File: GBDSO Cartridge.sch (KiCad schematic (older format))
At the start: 73 parts, among them J1 MJ-3523-SMT-TR, J2 MJ-3523-SMT-TR, J3 EdgeConnector, P1 100k, P2 100k, SW1 SW_SPDT, SW2 SW_SPDT, U1 TL062, U2 DS1267_SOIC, U3 TL062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

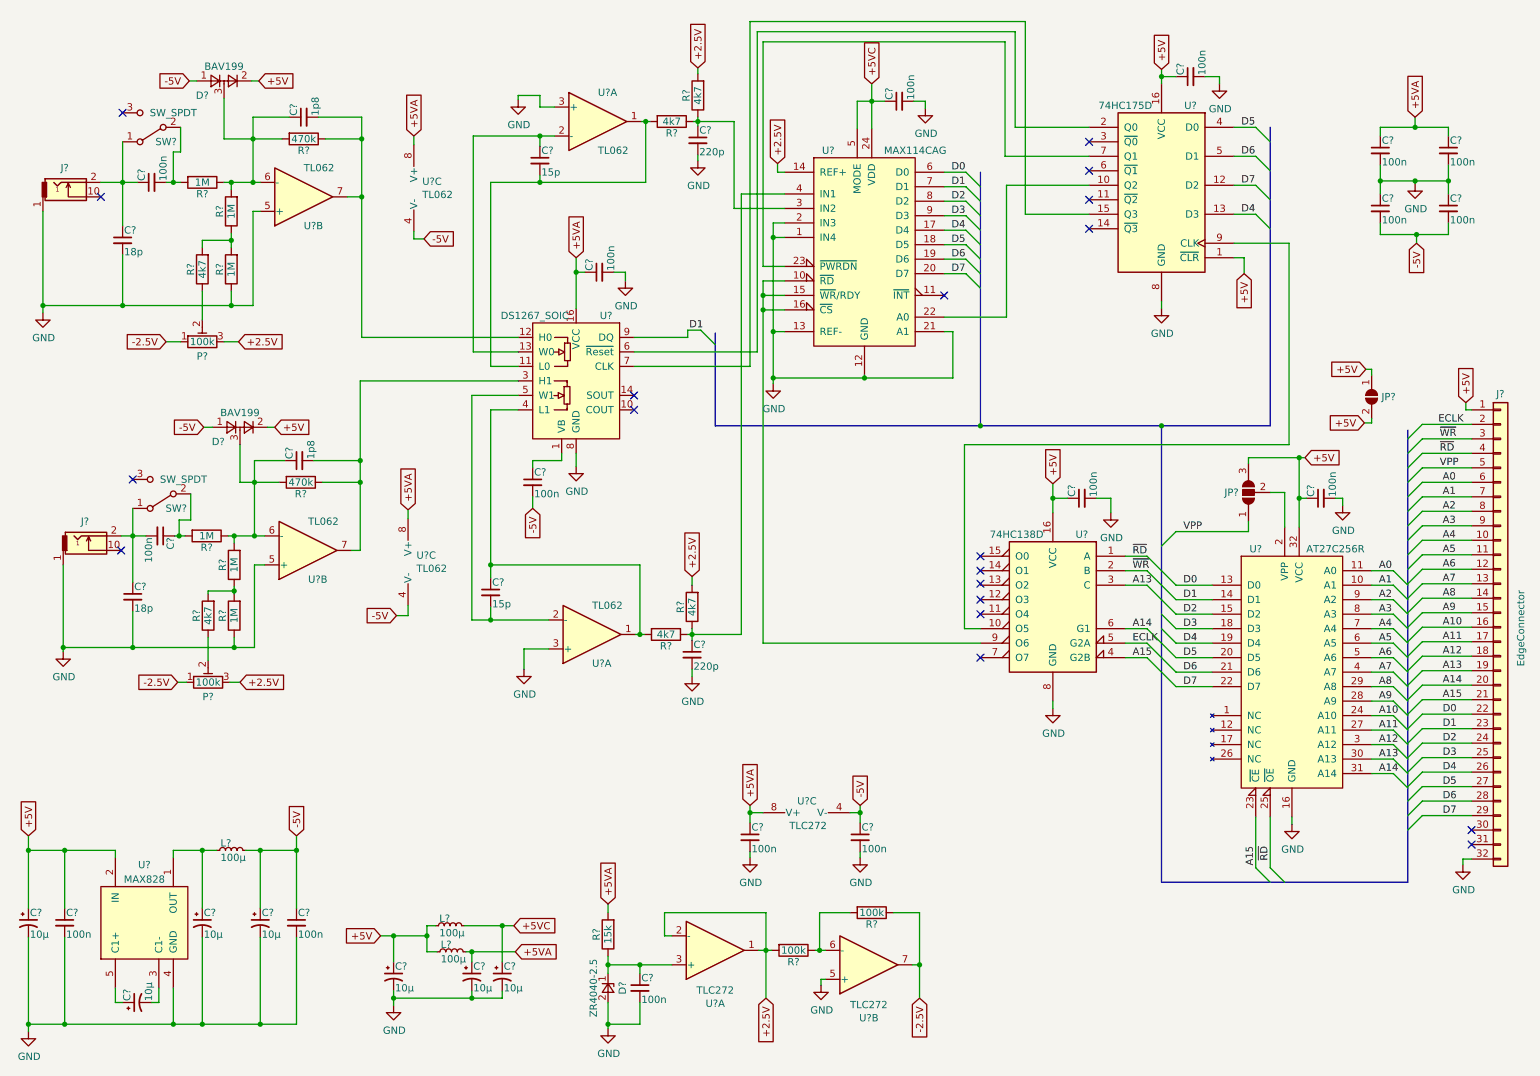
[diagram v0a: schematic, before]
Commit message: updated schematic, pcb, pictures and readme because I changed the GB connector to the Xunbeifang one
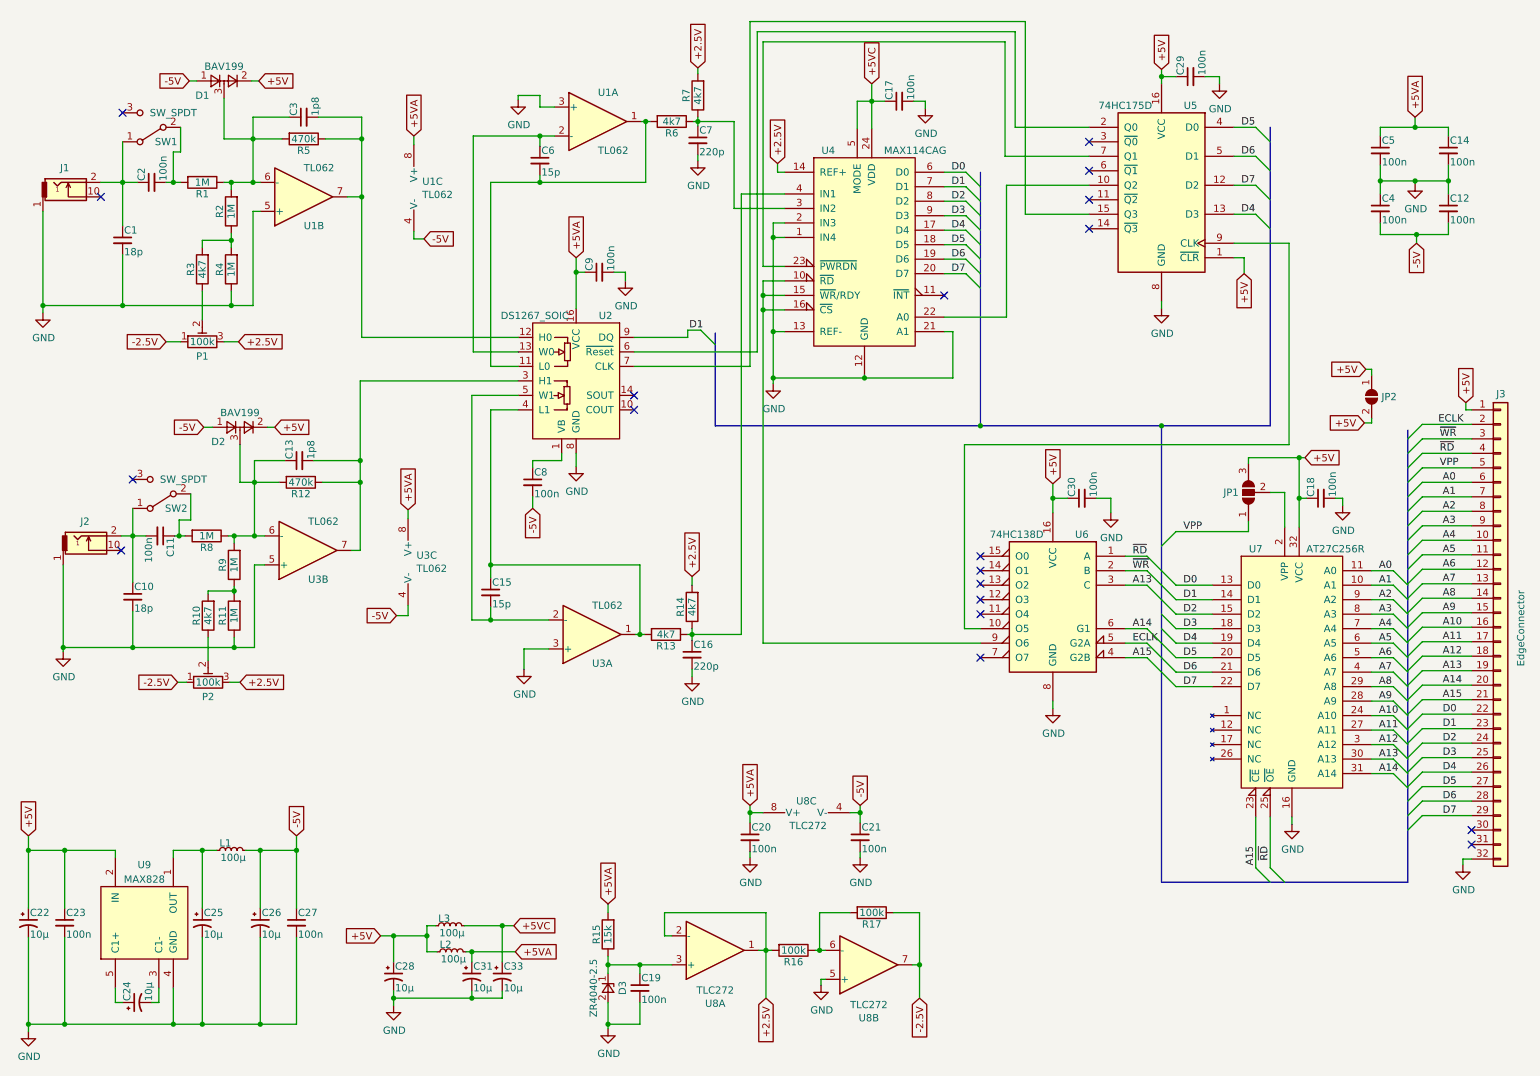
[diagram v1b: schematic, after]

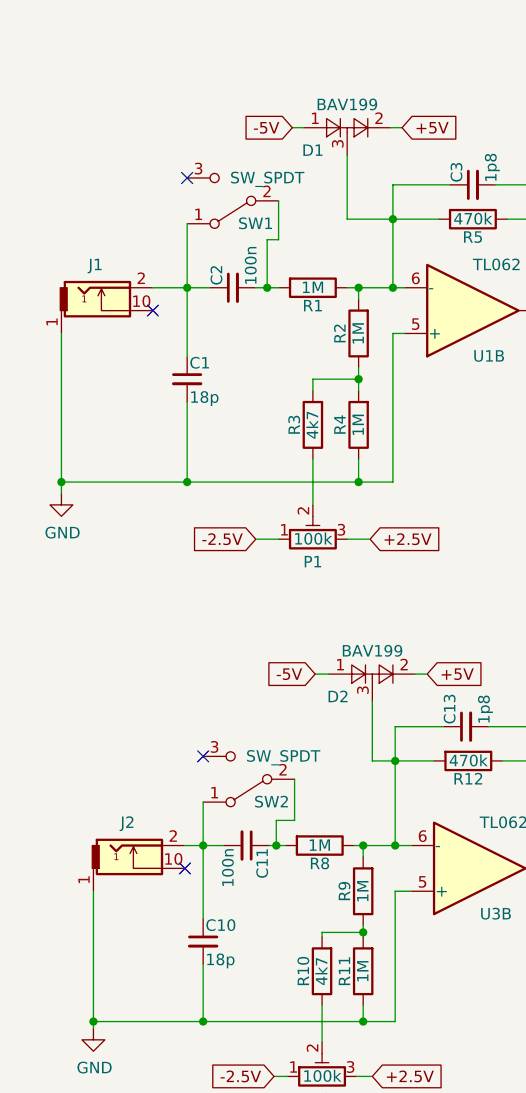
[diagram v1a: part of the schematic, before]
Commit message: Bunch of changes: fixed pin swap on DS1267_SOIC, fixed footprint of all uncorrect ICs, fixed footprint off the three inductors as they were too big. Because of the size change of the footprint of the ICs, some components had to be rearranged. Some routing improvements have been done, mostly on the right side of the board. I've added header pins to each channel input so that if anyone wants to use those instead of a 3.5mm audio jack they can. I've also added a few vias to the 3.5mm audio jack connectors and switches to hopefully help with mechanical stresses due to usage. That's all I can remember, should have split it into multiple commits...
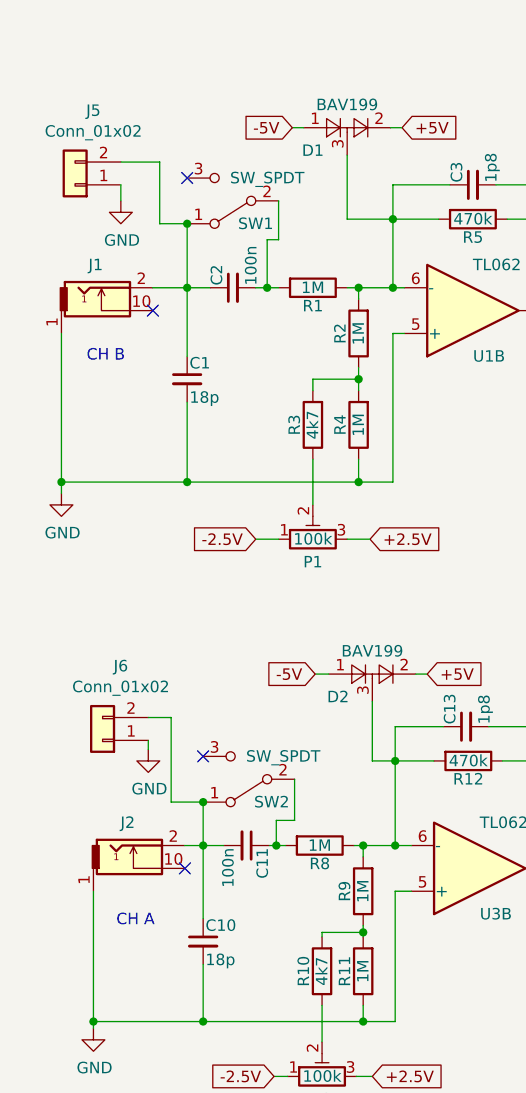
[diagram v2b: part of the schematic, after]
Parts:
- added J5, J6: Conn_01x02, Connector_PinHeader_2.54mm:PinHeader_1x02_P2.54mm_Horizontal, symbol Connector_Generic:Conn_01x02
- L1, L2, L3: footprint Inductor_SMD:L_1206_3216Metric -> Inductor_SMD:L_0805_2012Metric_Pad1.15x1.40mm_HandSolder
- U1, U3: footprint Package_SO:SO-8_5.3x6.2mm_P1.27mm -> Package_SO:SOIC-8_3.9x4.9mm_P1.27mm
- U2: footprint Package_SO:SOIC-16_3.9x9.9mm_P1.27mm -> Package_SO:SOIC-16W_7.5x10.3mm_P1.27mm
- U4: footprint Package_SO:SSOP-24_3.9x8.7mm_P0.635mm -> Package_SO:SSOP-24_5.3x8.2mm_P0.65mm
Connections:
- net GND: now also J5.1 (Pin_1), J6.1 (Pin_1)
- net at C1.1, C2.1, J1.2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: now also J5.2 (Pin_2)
- net at C10.1, C11.2, J2.2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: now also J6.2 (Pin_2)
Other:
- note added: "CH A"
- note added: "CH B"
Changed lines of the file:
@@
 EESchema Schematic File Version 4
 LIBS:GBDSO-cache
-EELAYER 26 0
+EELAYER 29 0
 EELAYER END
 $Descr A4 11693 8268
@@
 F 0 "U1" H 4610 1400 50  0000 L CNN
 F 1 "TL062" H 4610 1000 50  0000 L CNN
-F 2 "Package_SO:SO-8_5.3x6.2mm_P1.27mm" H 4610 1200 50  0001 C CNN
+F 2 "Package_SO:SOIC-8_3.9x4.9mm_P1.27mm" H 4610 1200 50  0001 C CNN
 F 3 "" H 4610 1200 50  0001 C CNN
 	1    4610 1200
@@
 F 0 "U1" H 2580 1920 50  0000 L CNN
 F 1 "TL062" H 2580 1520 50  0000 L CNN
-F 2 "Package_SO:SO-8_5.3x6.2mm_P1.27mm" H 2580 1720 50  0001 C CNN
+F 2 "Package_SO:SOIC-8_3.9x4.9mm_P1.27mm" H 2580 1720 50  0001 C CNN
 F 3 "" H 2580 1720 50  0001 C CNN
 	2    2580 1720
@@
 F 0 "U3" H 4570 4940 50  0000 L CNN
 F 1 "TL062" H 4570 4540 50  0000 L CNN
-F 2 "Package_SO:SO-8_5.3x6.2mm_P1.27mm" H 4570 4740 50  0001 C CNN
+F 2 "Package_SO:SOIC-8_3.9x4.9mm_P1.27mm" H 4570 4740 50  0001 C CNN
 F 3 "" H 4570 4740 50  0001 C CNN
 	1    4570 4740
@@
 F 0 "U3" H 2610 4360 50  0000 L CNN
 F 1 "TL062" H 2610 3960 50  0000 L CNN
-F 2 "Package_SO:SO-8_5.3x6.2mm_P1.27mm" H 2610 4160 50  0001 C CNN
+F 2 "Package_SO:SOIC-8_3.9x4.9mm_P1.27mm" H 2610 4160 50  0001 C CNN
 F 3 "" H 2610 4160 50  0001 C CNN
 	2    2610 4160
@@
 U 1 1 5C828B52
 P 4460 2990
+AR Path="/5C828B52" Ref="U2"  Part="1"
+AR Path="/5C8274B5/5C828B52" Ref="U2"  Part="1"
 F 0 "U2" H 4210 3440 50  0000 L CNN
 F 1 "DS1267_SOIC" H 4510 3440 50  0000 L CNN
-F 2 "Package_SO:SOIC-16_3.9x9.9mm_P1.27mm" H 5560 2540 50  0001 C CNN
+F 2 "Package_SO:SOIC-16W_7.5x10.3mm_P1.27mm" H 5560 2540 50  0001 C CNN
 F 3 "" H 4460 3040 50  0000 C CNN
 	1    4460 2990
@@
 F 0 "L1" V 2130 6230 50  0000 L CNN
 F 1 "100µ" V 2030 6130 50  0000 L CNN
-F 2 "Inductor_SMD:L_1206_3216Metric" H 2080 6230 50  0001 C CNN
+F 2 "Inductor_SMD:L_0805_2012Metric_Pad1.15x1.40mm_HandSolder" H 2080 6230 50  0001 C CNN
 F 3 "" H 2080 6230 50  0001 C CNN
 	1    2080 6230
@@
 F 0 "L2" V 3650 6930 50  0000 L CNN
 F 1 "100µ" V 3550 6830 50  0000 L CNN
-F 2 "Inductor_SMD:L_1206_3216Metric" H 3600 6930 50  0001 C CNN
+F 2 "Inductor_SMD:L_0805_2012Metric_Pad1.15x1.40mm_HandSolder" H 3600 6930 50  0001 C CNN
 F 3 "" H 3600 6930 50  0001 C CNN
 	1    3600 6930
@@
 F 0 "L3" V 3640 6750 50  0000 L CNN
 F 1 "100µ" V 3540 6650 50  0000 L CNN
-F 2 "Inductor_SMD:L_1206_3216Metric" H 3590 6750 50  0001 C CNN
+F 2 "Inductor_SMD:L_0805_2012Metric_Pad1.15x1.40mm_HandSolder" H 3590 6750 50  0001 C CNN
 F 3 "" H 3590 6750 50  0001 C CNN
 	1    3590 6750
@@
 F 0 "U4" H 6200 2800 50  0000 C CNN
 F 1 "MAX114CAG" H 6800 2800 50  0000 C CNN
-F 2 "Package_SO:SSOP-24_3.9x8.7mm_P0.635mm" H 7400 1350 50  0001 C CNN
+F 2 "Package_SO:SSOP-24_5.3x8.2mm_P0.65mm" H 7400 1350 50  0001 C CNN
 F 3 "" H 6450 550 50  0001 C CNN
 	1    6450 2100
@@
 NoConn ~ 1400 3670
 NoConn ~ 1330 1140
+$Comp
+L Connector_Generic:Conn_01x02 J5
+U 1 1 5CB7D891
+P 840 1170
+F 0 "J5" H 760 845 50  0000 C CNN
+F 1 "Conn_01x02" H 760 936 50  0000 C CNN
+F 2 "Connector_PinHeader_2.54mm:PinHeader_1x02_P2.54mm_Horizontal" H 840 1170 50  0001 C CNN
+F 3 "~" H 840 1170 50  0001 C CNN
+	1    840  1170
+	-1   0    0    1
+$EndComp
+$Comp
+L Connector_Generic:Conn_01x02 J6
+U 1 1 5CB7E2B7
+P 960 3600
+F 0 "J6" H 880 3275 50  0000 C CNN
+F 1 "Conn_01x02" H 880 3366 50  0000 C CNN
+F 2 "Connector_PinHeader_2.54mm:PinHeader_1x02_P2.54mm_Horizontal" H 960 3600 50  0001 C CNN
+F 3 "~" H 960 3600 50  0001 C CNN
+	1    960  3600
+	-1   0    0    1
+$EndComp
+Wire Wire Line
+	1400 3870 1260 3870
+Wire Wire Line
+	1260 3870 1260 3500
+Wire Wire Line
+	1260 3500 1160 3500
+Connection ~ 1400 3870
+$Comp
+L power:GND #PWR0127
+U 1 1 5CBDB355
+P 1160 3640
+F 0 "#PWR0127" H 1160 3390 50  0001 C CNN
+F 1 "GND" H 1165 3467 50  0000 C CNN
+F 2 "" H 1160 3640 50  0001 C CNN
+F 3 "" H 1160 3640 50  0001 C CNN
+	1    1160 3640
+	1    0    0    -1
+$EndComp
+Wire Wire Line
+	1160 3600 1160 3640
+Wire Wire Line
+	1040 1070 1210 1070
+Wire Wire Line
+	1210 1070 1210 1340
+Wire Wire Line
+	1210 1340 1330 1340
+Connection ~ 1330 1340
+$Comp
+L power:GND #PWR0128
+U 1 1 5CCF1BAC
+P 1040 1240
+F 0 "#PWR0128" H 1040 990 50  0001 C CNN
+F 1 "GND" H 1045 1067 50  0000 C CNN
+F 2 "" H 1040 1240 50  0001 C CNN
+F 3 "" H 1040 1240 50  0001 C CNN
+	1    1040 1240
+	1    0    0    -1
+$EndComp
+Wire Wire Line
+	1040 1170 1040 1240
+Text Notes 890  1950 0    50   ~ 0
+CH B
+Text Notes 1020 4420 0    50   ~ 0
+CH A
 Wire Bus Line
 	5420 2660 5420 3300
